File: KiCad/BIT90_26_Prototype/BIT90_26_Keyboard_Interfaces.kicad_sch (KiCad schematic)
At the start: 87 parts, among them J1 Cartridge, J12 Expansion2, J2 Expansion, J3 Joystick 1, J4 Joystick 2, J5 TAPE DUMP, J6 TAPE LOAD, J7 AUDIO OUT, SW10 CARAT, SW11 8, SW12 4, SW13 BS, SW14 DEL, SW15 2, SW16 6, SW17 ZERO, SW18 P, SW19 Y, SW2 UNDERSCORE, SW20 W, SW21 ], SW22 UP, SW23 ESC, SW24 R, SW25 I, SW26 [, SW27 U, SW28 E, SW29 RUBOUT, SW3 7, SW30 RIGHT, SW31 Q, SW32 T, SW33 O, SW34 SEMICOLON, SW35 H, SW36 S, SW37 AT, SW38 FWDSLASH, SW39 CAPS/LOWER, SW4 3, SW40 F, SW41 K, SW42 COLON, SW43 J, SW44 D, SW45 CR, SW46 PERIOD, SW47 A, SW48 G, SW49 L, SW5 BACKSLASH, SW50 N, SW51 V, SW52 X, SW53 M, SW54 COMMA, SW55 Z, SW56 C, SW57 B, SW58 L_SHIFT, SW59 R_SHIFT, SW6 INS, SW60 BIT, SW61 BASIC, SW62 LEFT, SW63 DOWN, SW64 CTRL, SW65 SPACE, SW66 FCTN, SW7 1, SW8 5, SW9 9, U25 LM393, U30 74LS145, U31 74LS244, U32 74LS174

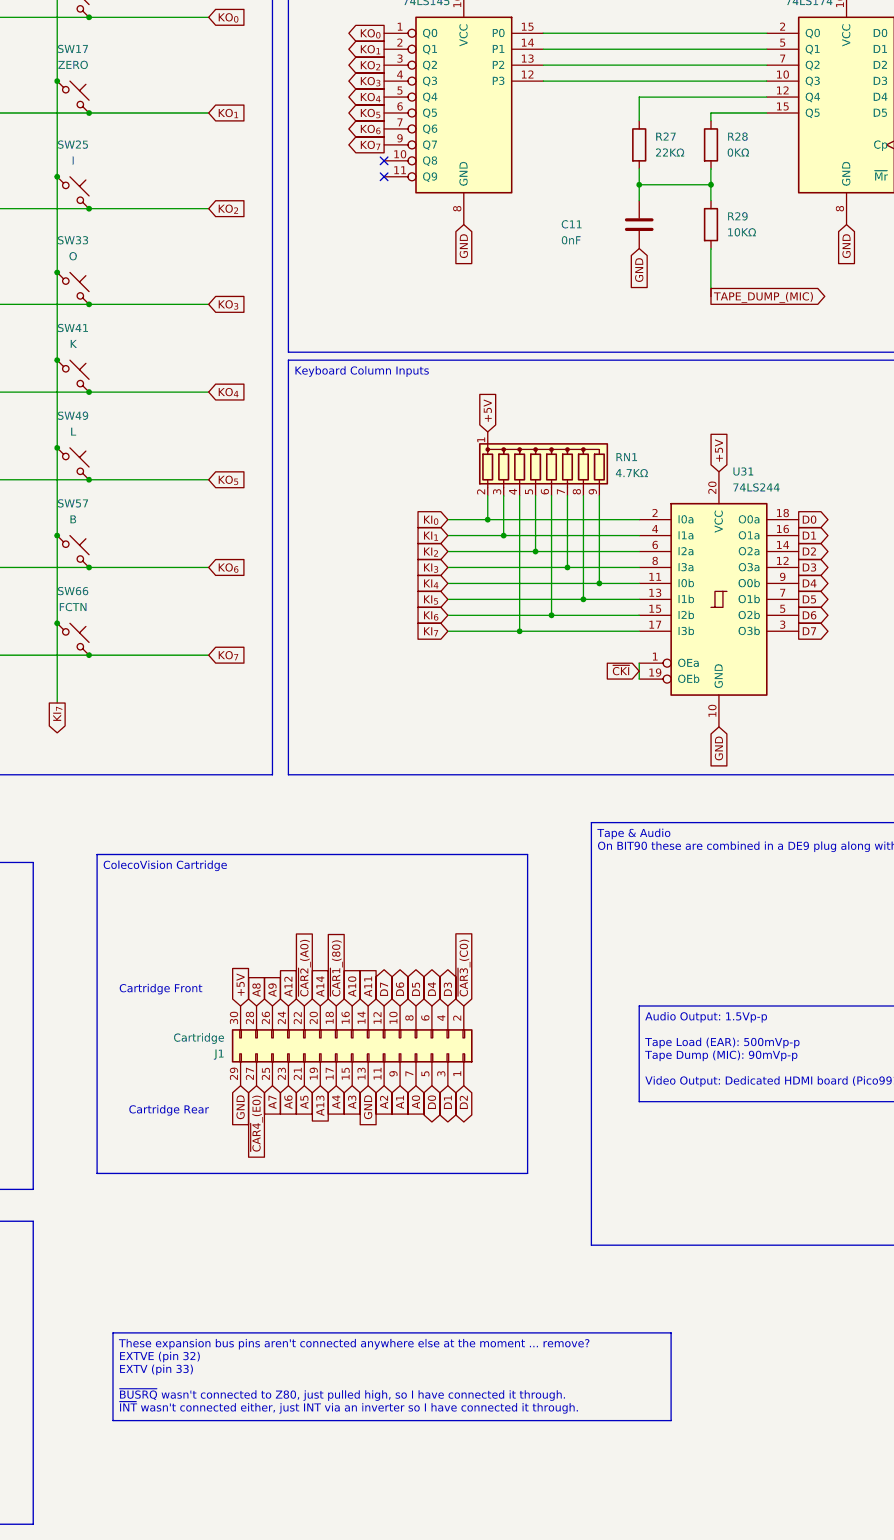
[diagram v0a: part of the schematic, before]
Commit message: Moved initial design to Prototype folder
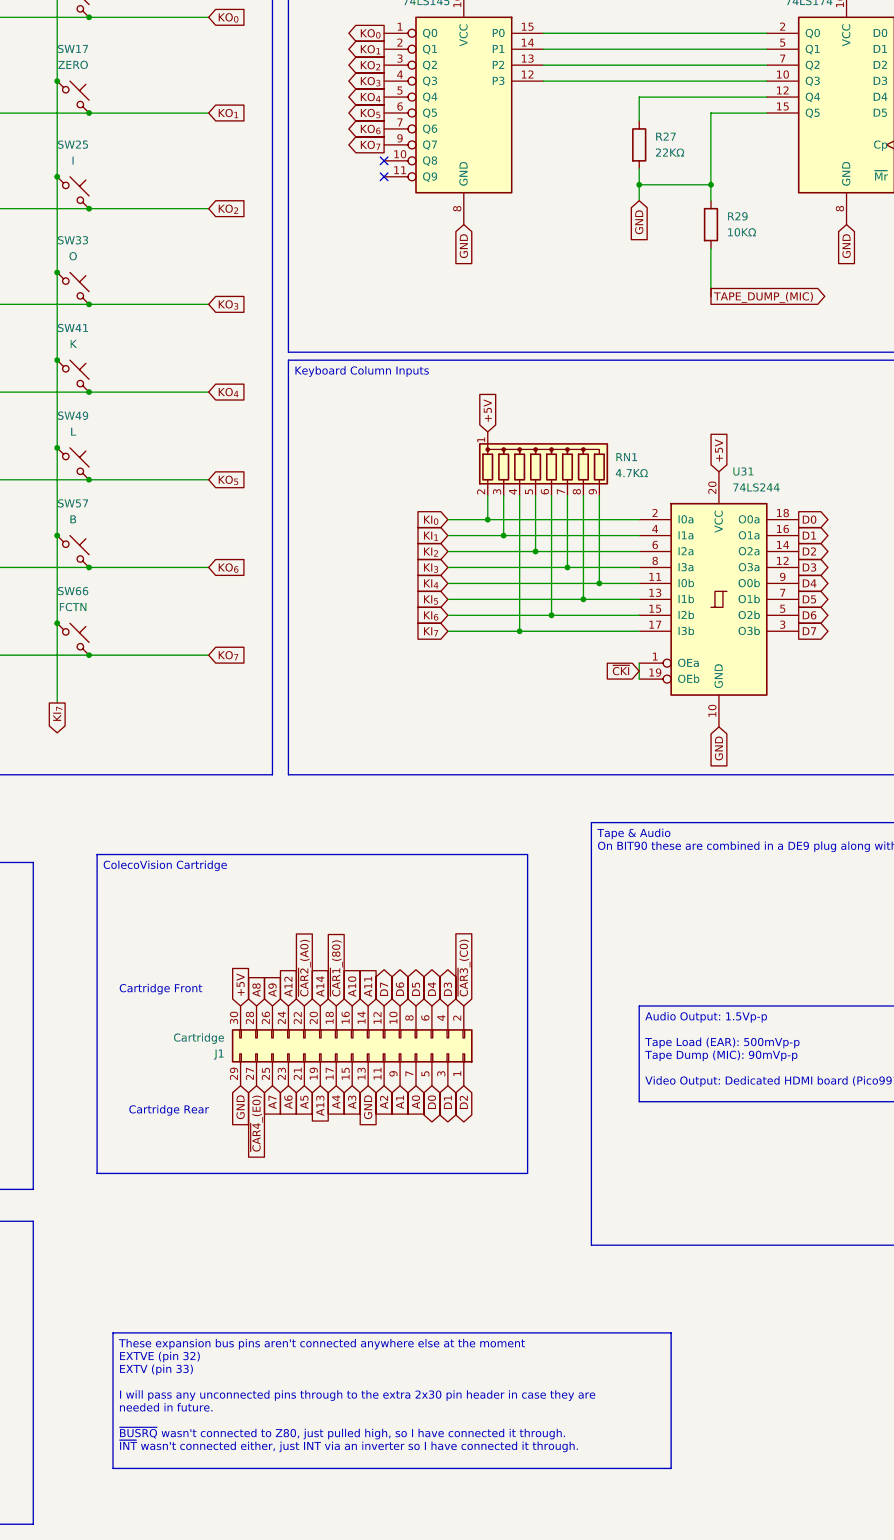
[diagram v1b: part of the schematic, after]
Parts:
- removed C11: 0nF, Capacitor_THT:C_Disc_D3.4mm_W2.1mm_P2.50mm, symbol Device:C
- removed R28: 0KΩ, Resistor_THT:R_Axial_DIN0207_L6.3mm_D2.5mm_P7.62mm_Horizontal, symbol Device:R
- D5, D6: footprint Diode_THT:D_DO-35_SOD27_P7.62mm_Horizontal -> Clueless_Engineer:D_DO-35_SOD27_P7.62mm_Horizontal
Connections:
- net GND: now also R27.2, R29.1, U32.15 (Q5)

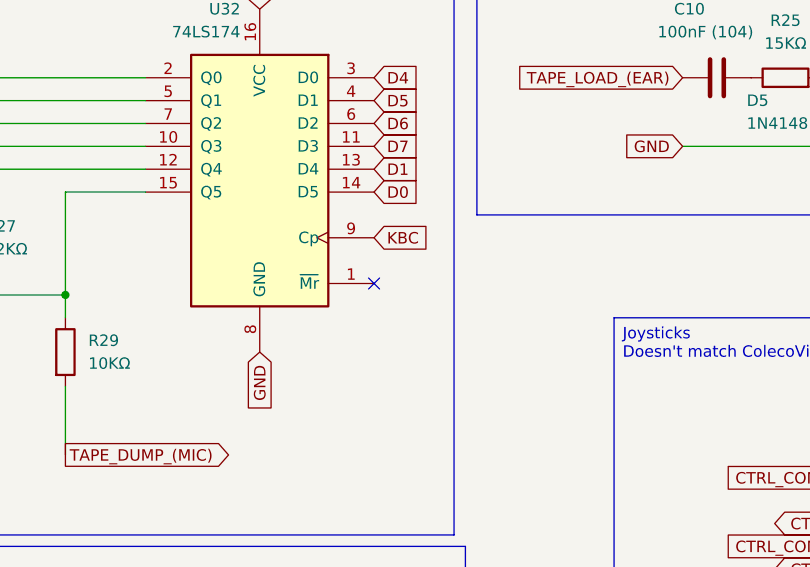
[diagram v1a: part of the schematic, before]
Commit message: Added more signal analysis to schematic
Would be nice to reduce the amount of glue logic
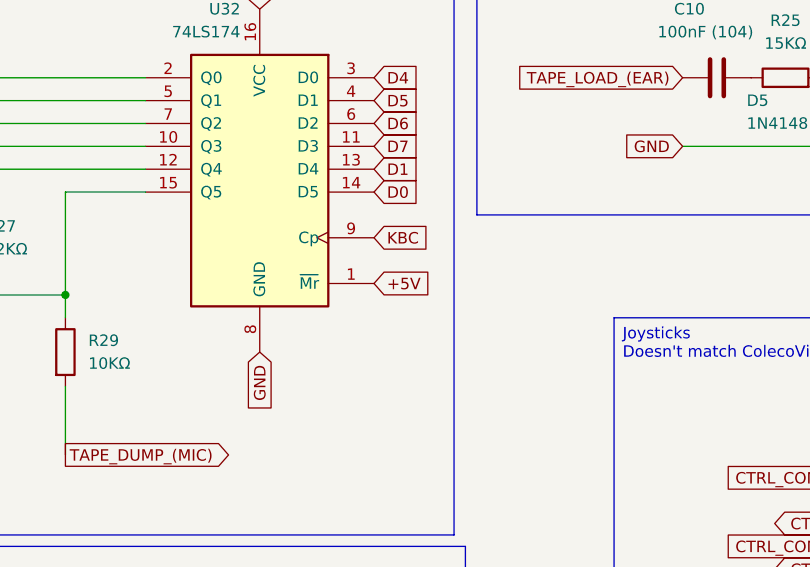
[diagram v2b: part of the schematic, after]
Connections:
- net +5V: now also U32.1 (~{Mr})
- no-connect marks 5 -> 4
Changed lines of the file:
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@@
 	)
 	(no_connect
-		(at 288.29 63.5)
-	)
-	(no_connect
 		(at 345.44 87.63)
 	)
@@
 			(effects
 				(font
+					(size 1.27 1.27)
+				)
+				(justify left)
+				(hide yes)
+			)
+		)
+	)
+	(global_label "+5V"
+		(shape input)
+		(at 288.29 63.5 0)
+		(fields_autoplaced yes)
+		(effects
+			(font
+				(size 1.27 1.27)
+			)
+			(justify left)
+		)
+		(property "Intersheetrefs" "${INTERSHEET_REFS}"
+			(at 295.1457 63.5 0)
+			(effects
+				(font
